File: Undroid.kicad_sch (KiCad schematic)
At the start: 41 parts

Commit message: Finishing routing.
Signed-off-by: Amlal EL Mahrouss <amlalelmahrouss@icloud.com>
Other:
- note added: "NOT HERE!"
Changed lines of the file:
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@@
+		)
+	)
+	(text "NOT HERE!"
+		(exclude_from_sim yes)
+		(at 373.38 108.204 0)
+		(effects
+			(font
+				(size 5.08 5.08)
+			)
 		)
 	)

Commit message: pcb-master: Start of step 2: Finish and improve routing of motherboard.
Signed-off-by: Amlal EL Mahrouss <amlalelmahrouss@icloud.com>
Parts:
- removed R_VDD_3V3: R, Resistor_SMD:R_0201_0603Metric, symbol Device:R
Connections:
- net GND: no longer SIM_CHIP1.39 (~{PWRKEY})
- net GSM_PWR_N: now reaches MBCI_IO1.6 (Pin_6)
- net GSM_PWR_N: now also SIM_CHIP1.39 (~{PWRKEY})
- net GSM_RST_N: now reaches MBCI_IO1.7 (Pin_7)
- net GSM_RST_N: now also SIM_CHIP1.28 (~{RESET})
- no-connect marks 71 -> 69
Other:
- note added: "LTE module"
- note removed: "GPRS Modem"
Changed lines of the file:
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@@
 	)
 	(no_connect
+		(at 66.04 67.31)
+	)
+	(no_connect
 		(at 245.11 292.1)
 	)
@@
 	)
 	(no_connect
-		(at 45.72 102.87)
-	)
-	(no_connect
 		(at 538.48 83.82)
 	)
@@
 	)
 	(no_connect
-		(at 260.35 386.08)
-	)
-	(no_connect
 		(at 195.58 227.33)
 	)
@@
 	)
 	(no_connect
-		(at 262.89 386.08)
-	)
-	(no_connect
 		(at 467.36 165.1)
 	)
@@
 	(wire
 		(pts
-			(xy 62.23 57.15) (xy 62.23 60.96)
-		)
-		(stroke
-			(width 0)
-			(type default)
-		)
-	)
-	(wire
-		(pts
 			(xy 123.19 316.23) (xy 123.19 322.58)
 		)
@@
 	(wire
 		(pts
-			(xy 62.23 60.96) (xy 66.04 60.96)
+			(xy 140.97 229.87) (xy 140.97 232.41)
 		)
 		(stroke
@@
 	(wire
 		(pts
-			(xy 140.97 229.87) (xy 140.97 232.41)
+			(xy 107.95 72.39) (xy 107.95 41.91)
 		)
 		(stroke
@@
 	(wire
 		(pts
-			(xy 107.95 72.39) (xy 107.95 41.91)
+			(xy 118.11 204.47) (xy 125.73 204.47)
 		)
 		(stroke
@@
 	(wire
 		(pts
-			(xy 118.11 204.47) (xy 125.73 204.47)
+			(xy 561.34 187.96) (xy 567.69 187.96)
 		)
 		(stroke
@@
 	(wire
 		(pts
-			(xy 561.34 187.96) (xy 567.69 187.96)
+			(xy 365.76 381) (xy 370.84 381)
 		)
 		(stroke
@@
 	(wire
 		(pts
-			(xy 365.76 381) (xy 370.84 381)
+			(xy 40.64 102.87) (xy 45.72 102.87)
 		)
 		(stroke
@@
 	(wire
 		(pts
-			(xy 66.04 60.96) (xy 66.04 67.31)
-		)
-		(stroke
-			(width 0)
-			(type default)
-		)
-	)
-	(wire
-		(pts
 			(xy 107.95 298.45) (xy 113.03 298.45)
 		)
@@
 	(wire
 		(pts
-			(xy 62.23 46.99) (xy 62.23 49.53)
-		)
-		(stroke
-			(width 0)
-			(type default)
-		)
-	)
-	(wire
-		(pts
 			(xy 350.52 287.02) (xy 363.22 287.02)
 		)
@@
 	(wire
 		(pts
-			(xy 30.48 100.33) (xy 45.72 100.33)
+			(xy 40.64 100.33) (xy 45.72 100.33)
 		)
 		(stroke
@@
 		)
 	)
-	(text "GPRS Modem"
+	(text "LTE module"
 		(exclude_from_sim yes)
 		(at 132.08 26.924 0)
@@
 		)
 	)
+	(global_label "GSM_PWR_N"
+		(shape input)
+		(at 262.89 386.08 90)
+		(fields_autoplaced yes)
+		(effects
+			(font
+				(size 1.27 1.27)
+			)
+			(justify left)
+		)
+		(property "Intersheetrefs" "${INTERSHEET_REFS}"
+			(at 262.89 371.9068 90)
+			(effects
+				(font
+					(size 1.27 1.27)
+				)
+				(justify left)
+				(hide yes)
+			)
+		)
+	)
 	(global_label "3.3V"
 		(shape input)
@@
 		)
 	)
-	(global_label "VBUS_USBC"
-		(shape output)
-		(at 62.23 46.99 90)
-		(fields_autoplaced yes)
-		(effects
-			(font
-				(size 1.27 1.27)
-			)
-			(justify left)
-		)
-		(property "Intersheetrefs" "${INTERSHEET_REFS}"
-			(at 62.23 33.0586 90)
-			(effects
-				(font
-					(size 1.27 1.27)
-				)
-				(justify left)
-				(hide yes)
-			)
-		)
-	)
 	(global_label "RAM_LDQS"
 		(shape input)
@@
 		)
 	)
+	(global_label "GSM_RST_N"
+		(shape input)
+		(at 260.35 386.08 90)
+		(fields_autoplaced yes)
+		(effects
+			(font
+				(size 1.27 1.27)
+			)
+			(justify left)
+		)
+		(property "Intersheetrefs" "${INTERSHEET_REFS}"
+			(at 260.35 372.4511 90)
+			(effects
+				(font
+					(size 1.27 1.27)
+				)
+				(justify left)
+				(hide yes)
+			)
+		)
+	)
 	(global_label "SD_DAT1"
 		(shape input)
@@
 		)
 	)
+	(global_label "GSM_PWR_N"
+		(shape input)
+		(at 40.64 100.33 180)
+		(fields_autoplaced yes)
+		(effects
+			(font
+				(size 1.27 1.27)
+			)
+			(justify right)
+		)
+		(property "Intersheetrefs" "${INTERSHEET_REFS}"
+			(at 26.4668 100.33 0)
+			(effects
+				(font
+					(size 1.27 1.27)
+				)
+				(justify right)
+				(hide yes)
+			)
+		)
+	)
 	(global_label "VBUS_USBC"
 		(shape output)
@@
 		)
 	)
+	(global_label "GSM_RST_N"
+		(shape input)
+		(at 40.64 102.87 180)
+		(fields_autoplaced yes)
+		(effects
+			(font
+				(size 1.27 1.27)
+			)
+			(justify right)
+		)
+		(property "Intersheetrefs" "${INTERSHEET_REFS}"
+			(at 27.0111 102.87 0)
+			(effects
+				(font
+					(size 1.27 1.27)
+				)
+				(justify right)
+				(hide yes)
+			)
+		)
+	)
 	(global_label "RTC_OUT"
 		(shape input)
@@
 	)
 	(symbol
-		(lib_id "power:GND")
-		(at 30.48 100.33 270)
-		(unit 1)
-		(exclude_from_sim no)
-		(in_bom yes)
-		(on_board yes)
-		(dnp no)
-		(fields_autoplaced yes)
-		(property "Reference" "#PWR062"
-			(at 24.13 100.33 0)
-			(effects
-				(font
-					(size 1.27 1.27)
-				)
-				(hide yes)
-			)
-		)
-		(property "Value" "GND"
-			(at 26.67 100.3299 90)
-			(effects
-				(font
-					(size 1.27 1.27)
-				)
-				(justify right)
-			)
-		)
-		(property "Footprint" ""
-			(at 30.48 100.33 0)
-			(effects
-				(font
-					(size 1.27 1.27)
-				)
-				(hide yes)
-			)
-		)
-		(property "Datasheet" ""
-			(at 30.48 100.33 0)
-			(effects
-				(font
-					(size 1.27 1.27)
-				)
-				(hide yes)
-			)
-		)
-		(property "Description" "Power symbol creates a global label with name \"GND\" , ground"
-			(at 30.48 100.33 0)
-			(effects
-				(font
-					(size 1.27 1.27)
-				)
-				(hide yes)
-			)
-		)
-		(pin "1"
-		)
-		(instances
-			(project "Undroid"
-				(path "/5d3a3bfa-72d2-42b8-bac3-6ac6fe44d852"
-					(reference "#PWR062")
-					(unit 1)
-				)
-			)
-		)
-	)
-	(symbol
 		(lib_id "Connector:USB_C_Receptacle_PowerOnly_6P")
 		(at 48.26 215.9 90)
@@
 					(unit 1)
 				)
-			)
-		)
-	)
-	(symbol
-		(lib_id "Device:R")
-		(at 62.23 53.34 0)
-		(unit 1)
-		(exclude_from_sim no)
-		(in_bom yes)
-		(on_board yes)
-		(dnp no)
-		(fields_autoplaced yes)
-		(property "Reference" "R_VDD_3V3"
-			(at 64.77 52.0699 0)
-			(effects
-				(font
-					(size 1.27 1.27)
-				)
-				(justify left)
-			)
-		)
-		(property "Value" "R"
-			(at 64.77 54.6099 0)
-			(effects
-				(font
-					(size 1.27 1.27)
-				)
-				(justify left)
-			)
-		)
-		(property "Footprint" "Resistor_SMD:R_0201_0603Metric"
-			(at 60.452 53.34 90)
-			(effects
-				(font
-					(size 1.27 1.27)
-				)
-				(hide yes)
-			)
-		)
-		(property "Datasheet" "~"
-			(at 62.23 53.34 0)
-			(effects
-				(font
-					(size 1.27 1.27)
-				)
-				(hide yes)
-			)
-		)
-		(property "Description" "Resistor"
-			(at 62.23 53.34 0)
-			(effects
-				(font
-					(size 1.27 1.27)
-				)
-				(hide yes)
-			)
-		)
-		(pin "1"
-		)
-		(pin "2"
-		)
-		(instances
-			(project "Undroid"
-				(path "/5d3a3bfa-72d2-42b8-bac3-6ac6fe44d852"
-					(reference "R_VDD_3V3")
-					(unit 1)
-				)

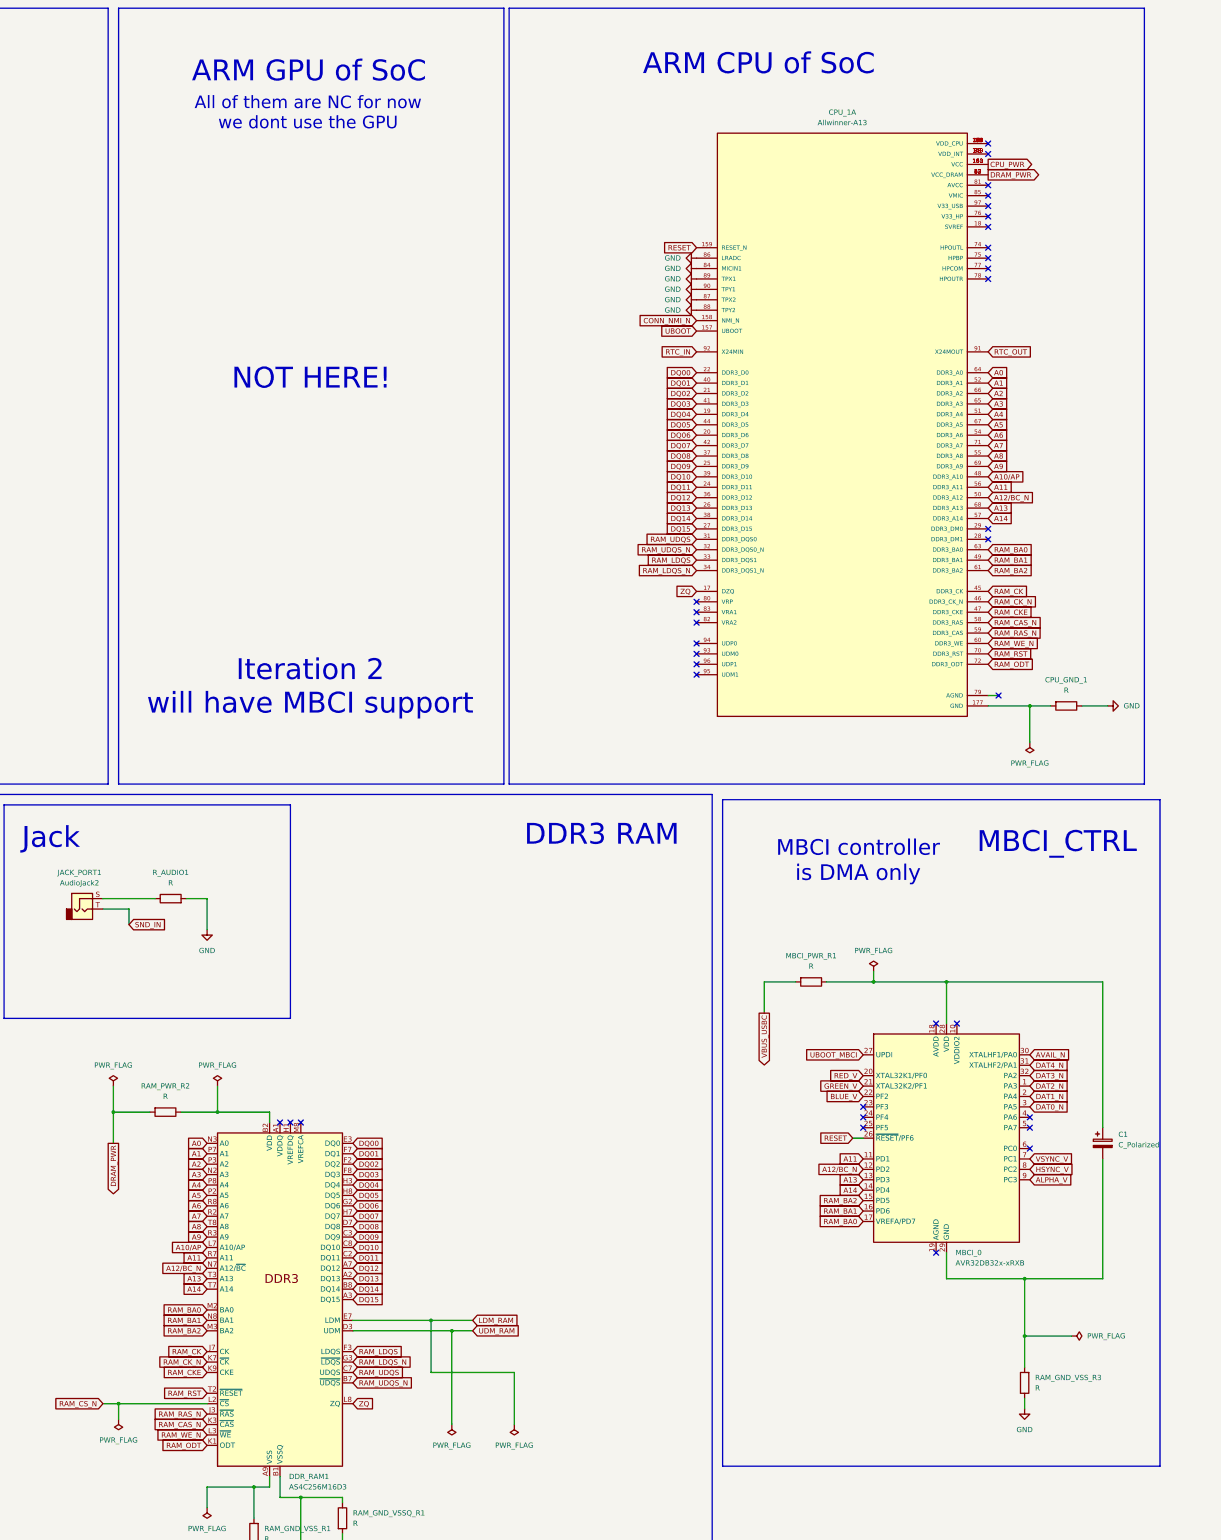
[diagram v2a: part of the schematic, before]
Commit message: FIX: Schematic and PCB, Improved those and regenerated zones as well.
Signed-off-by: Amlal EL Mahrouss <amlalelmahrouss@icloud.com>
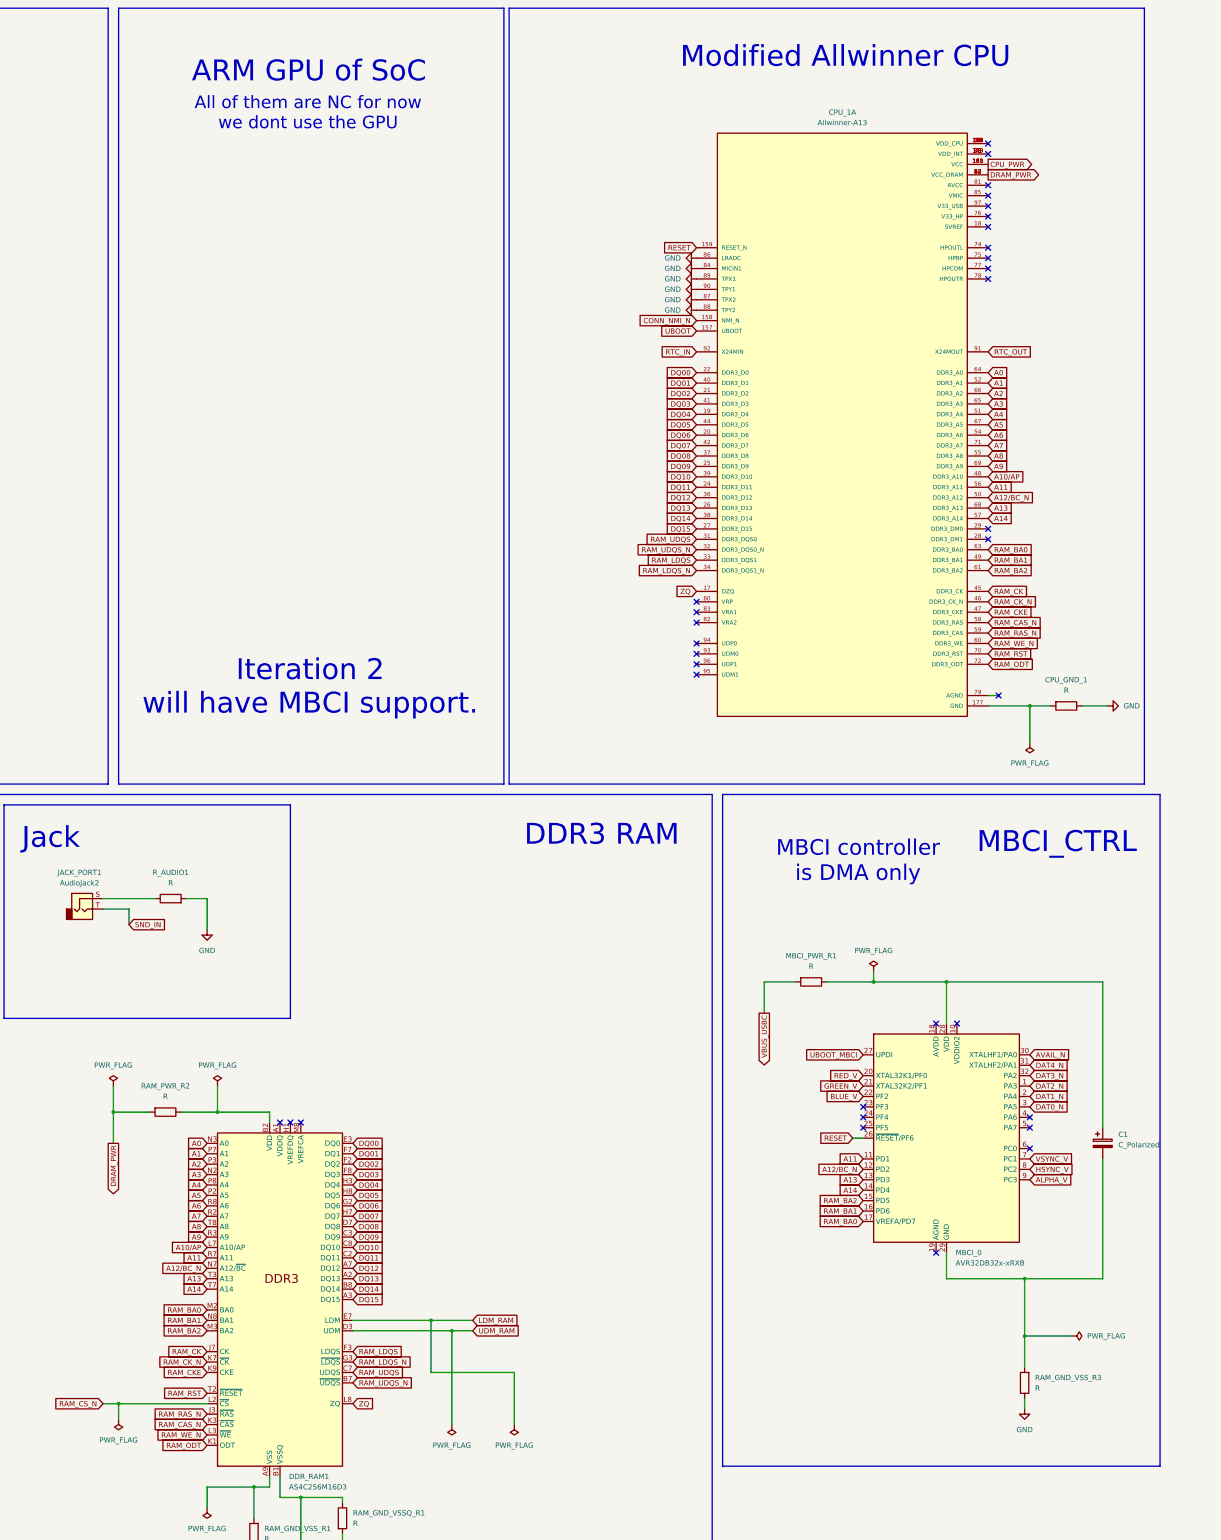
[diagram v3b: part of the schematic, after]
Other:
- note added: "Iteration 2 will have MBCI support."
- note added: "Modified Allwinner CPU"
- note removed: "ARM CPU of SoC"
- note removed: "Iteration 2 will have MBCI support"
- note removed: "NOT HERE!"
- company: Zeta -> Radio Corporation of Morocco
- title: Phone motherboard -> ZETA-0001
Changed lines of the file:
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@@
 	(paper "A2")
 	(title_block
-		(title "Phone motherboard")
+		(title "ZETA-0001")
 		(date "2024-06-19")
 		(rev "10")
-		(company "Zeta")
+		(company "Radio Corporation of Morocco")
 	)
 	(junction
@@
 	)
 	(rectangle
-		(start 473.71 210.82)
+		(start 473.71 209.55)
 		(end 580.39 373.38)
 		(stroke
@@
 		)
 	)
-	(text "Iteration 2\nwill have MBCI support"
+	(text "Iteration 2\nwill have MBCI support."
 		(exclude_from_sim yes)
 		(at 373.126 183.388 0)
@@
 		)
 	)
-	(text "ARM CPU of SoC"
+	(text "Modified Allwinner CPU"
 		(exclude_from_sim yes)
-		(at 482.6 31.496 0)
+		(at 503.682 29.718 0)
 		(effects
 			(font
@@
 		(effects
 			(font
-				(size 5.08 5.08)
-			)
-		)
-	)
-	(text "NOT HERE!"
-		(exclude_from_sim yes)
-		(at 373.38 108.204 0)
-		(effects
-			(font

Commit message: FIX: provide ohm values of resistors in schematic, as well as resistor for CC1.
Signed-off-by: Amlal EL Mahrouss <amlalelmahrouss@icloud.com>
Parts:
- removed C1: C_Polarized, Capacitor_Tantalum_SMD:CP_EIA-2012-12_Kemet-R, symbol Device:C_Polarized
- added C1: 100n, symbol Device:C
- CC1_R1, CC2_R1, CPU_GND_1, GND_BRIDGE_R1, GND_R1, MBCI_PWR_R1, MCU_PWR_R1, MCU_PWR_R2, NETLIGHT_R1, RAM_GND_VSSQ_R1, RAM_GND_VSS_R1, RAM_GND_VSS_R3, RAM_PWR_R2, RVSS_S_1, R_AUDIO1, VBAT_R1, VCC_FL_1, VCC_FL_2, VCC_S_1, VSS_FL_1, VSS_FL_2, VSS_SD_VDD1, VSS_SD_VSS1: value R -> 15OR
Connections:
- net at MBCI_0.28 (VDD), MBCI_PWR_R1.1: now also C1.1
- net at MBCI_0.29 (GND), MBCI_0.33 (GND), RAM_GND_VSS_R3.2: now also C1.2
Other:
- company: Radio Corporation of Morocco -> Zeta Electronics NV

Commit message: IMP: New RESET_N pin
Signed-off-by: Amlal EL Mahrouss <amlalelmahrouss@icloud.com>
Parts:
- removed CPU_1: Allwinner-A13, Allwinner:QFP40P2200X2200X160-177N, symbol Allwinner:Allwinner-A13
- added CPU_1A1, GPU_A1: Allwinner-A13, Allwinner-A13:QFP40P2200X2200X160-177N, symbol Allwinner:Allwinner-A13
- C1: footprint (none) -> Capacitor_SMD:C_0402_1005Metric
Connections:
- net A0: now also CPU_1A1.64 (DDR3_A0)
- net A1: now also CPU_1A1.52 (DDR3_A1)
- net A10/AP: now also CPU_1A1.48 (DDR3_A10)
- net A11: now also CPU_1A1.56 (DDR3_A11)
- net A12/BC_N: now also CPU_1A1.50 (DDR3_A12)
- net A13: now also CPU_1A1.68 (DDR3_A13)
- net A14: now also CPU_1A1.57 (DDR3_A14)
- net A2: now also CPU_1A1.66 (DDR3_A2)
- net A3: now also CPU_1A1.65 (DDR3_A3)
- net A4: now also CPU_1A1.51 (DDR3_A4)
- net A5: now also CPU_1A1.67 (DDR3_A5)
- net A6: now also CPU_1A1.54 (DDR3_A6)
- net A7: now also CPU_1A1.71 (DDR3_A7)
- net A8: now also CPU_1A1.55 (DDR3_A8)
- net A9: now also CPU_1A1.69 (DDR3_A9)
- net CONN_NMI_N: now also CPU_1A1.158 (NMI_N)
- net CPU_PWR: now also CPU_1A1.100 (VCC), CPU_1A1.109 (VDD_INT), CPU_1A1.11 (VDD_CPU), CPU_1A1.142 (VCC), CPU_1A1.149 (VDD_INT), CPU_1A1.156 (VDD_CPU), CPU_1A1.16 (VDD_CPU), CPU_1A1.163 (VCC), CPU_1A1.164 (VDD_CPU), CPU_1A1.169 (VDD_CPU), CPU_1A1.173 (VDD_CPU), CPU_1A1.35 (VDD_INT), CPU_1A1.4 (VDD_CPU), CPU_1A1.5 (VCC), CPU_1A1.73 (VDD_INT), CPU_1A1.9 (VDD_CPU), CPU_1A1.98 (VDD_INT)
- net DQ00: now also CPU_1A1.22 (DDR3_D0)
- net DQ01: now also CPU_1A1.40 (DDR3_D1)
- net DQ02: now also CPU_1A1.21 (DDR3_D2)
- net DQ03: now also CPU_1A1.41 (DDR3_D3)
- net DQ04: now also CPU_1A1.19 (DDR3_D4)
- net DQ05: now also CPU_1A1.44 (DDR3_D5)
- net DQ06: now also CPU_1A1.20 (DDR3_D6)
- net DQ07: now also CPU_1A1.42 (DDR3_D7)
- net DQ08: now also CPU_1A1.37 (DDR3_D8)
- net DQ09: now also CPU_1A1.25 (DDR3_D9)
- net DQ10: now also CPU_1A1.39 (DDR3_D10)
- net DQ11: now also CPU_1A1.24 (DDR3_D11)
- net DQ12: now also CPU_1A1.36 (DDR3_D12)
- net DQ13: now also CPU_1A1.26 (DDR3_D13)
- net DQ14: now also CPU_1A1.38 (DDR3_D14)
- net DQ15: now also CPU_1A1.27 (DDR3_D15)
- net DRAM_PWR: now also CPU_1A1.23 (VCC_DRAM), CPU_1A1.30 (VCC_DRAM), CPU_1A1.43 (VCC_DRAM), CPU_1A1.53 (VCC_DRAM), CPU_1A1.62 (VCC_DRAM)
- net GND: now also CPU_1A1.84 (MICIN1), CPU_1A1.86 (LRADC), CPU_1A1.87 (TPX2), CPU_1A1.88 (TPY2), CPU_1A1.89 (TPX1), CPU_1A1.90 (TPY1)
- net RAM_BA0: now also CPU_1A1.63 (DDR3_BA0)
- net RAM_BA1: now also CPU_1A1.49 (DDR3_BA1)
- net RAM_BA2: now also CPU_1A1.61 (DDR3_BA2)
- net RAM_CAS_N: now also CPU_1A1.58 (DDR3_RAS)
- net RAM_CK: now also CPU_1A1.45 (DDR3_CK)
- net RAM_CKE: now also CPU_1A1.47 (DDR3_CKE)
- net RAM_CK_N: now also CPU_1A1.46 (DDR3_CK_N)
- net RAM_LDQS: now also CPU_1A1.33 (DDR3_DQS1)
- net RAM_LDQS_N: now also CPU_1A1.34 (DDR3_DQS1_N)
- net RAM_ODT: now also CPU_1A1.72 (DDR3_ODT)
- net RAM_RAS_N: now also CPU_1A1.59 (DDR3_CAS)
- net RAM_RST: now also CPU_1A1.70 (DDR3_RST)
- net RAM_UDQS: now also CPU_1A1.31 (DDR3_DQS0)
- net RAM_UDQS_N: now also CPU_1A1.32 (DDR3_DQS0_N)
- net RAM_WE_N: now also CPU_1A1.60 (DDR3_WE)
- net RTC_IN: now also CPU_1A1.92 (X24MIN)
- net RTC_OUT: now also CPU_1A1.91 (X24MOUT)
- net UBOOT: now also CPU_1A1.157 (UBOOT)
- net ZQ: now also CPU_1A1.17 (DZQ)
- net at CPU_GND_1.2: now also CPU_1A1.177 (GND)
- net RESET renamed RESET_N
- net RESET_N: now also CPU_1A1.159 (RESET_N)
- no-connect marks 69 -> 143
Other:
- note added: "And reset circuit"
- note added: "SUNXI A13 CPU"
- note added: "SUNXI A13 GPU"
- note removed: "ARM GPU of SoC"
- note removed: "All of them are NC for now we dont use the GPU"
- note removed: "Iteration 2 will have MBCI support."
- note removed: "Modified Allwinner CPU"
- moved on the sheet: VBAT_R1
